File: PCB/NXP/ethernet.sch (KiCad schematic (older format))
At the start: 40 parts, among them P1 HR911105A, U1 LAN8720A-CP, U2 SI502

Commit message: #45 added PoE connector (P1) and expansion (P3).
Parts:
- removed P1: HR911105A, symbol CONN_14
- added P1: SI-52003-F, ~, symbol CONN_17
- added P3: PoE, ~, symbol CONN_7
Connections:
- net labels added: +24V, +5V
- wire segments 114 -> 131
- no-connect marks 2 -> 3
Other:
- note added: "Se agregan entradas de +5V y +24V para alimentar la CIAA\na través de PoE. Es necesario diseñar una expansión tal que, \nademás de la fuente de tensión, disponga de diodos de \nprotección para no dañarla si se alimenta la CIAA en forma \ntradicional. Se sugiere usar diodos PMEG3020EH como en la \nfuente de alimentación. A su vez es necesario que cada entrada\nPoE tenga un puente rectificador de o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"
- note added: "TD+\nCT\nTD-\nRD+\nRD-\nNC\nNC\nVC+\nVC-\nVC+\nVC-\nLED1_A\nLED1_K\nLED2_A\nLED2_K\nSHIELD\nSHIELD"
- note removed: "Verificar disponibilidad del conector Ethernet.\nAlternativa: Pulse J0011D01BNL."
- moved on the sheet: R17, R18
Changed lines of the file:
@@
 Sheet 3 12
 Title "CIAA Ethernet"
-Date "18 aug 2014"
+Date "19 aug 2014"
 Rev "1.0"
 Comp ""
@@
 $EndComp
 $Comp
-L CONN_14 P1
-U 1 1 529F7478
-P 10000 3950
-F 0 "P1" V 9970 3950 60  0000 C CNN
-F 1 "HR911105A" V 10080 3950 60  0000 C CNN
-F 2 "" H 10000 3950 60  0000 C CNN
-F 3 "" H 10000 3950 60  0000 C CNN
-	1    10000 3950
-	1    0    0    -1
-$EndComp
-$Comp
 L R R3
 U 1 1 529F75AC
@@
 	7100 3900 7550 3900
 Wire Wire Line
-	7550 3900 7550 3400
-Wire Wire Line
-	7550 3400 9650 3400
+	7550 3900 7550 3500
+Wire Wire Line
+	7550 3500 9650 3500
 Wire Wire Line
 	7100 4000 7650 4000
 Wire Wire Line
-	7650 3500 7650 4300
-Wire Wire Line
-	7650 3500 9650 3500
-Wire Wire Line
 	7100 4100 7750 4100
 Wire Wire Line
-	7750 4100 7750 3800
-Wire Wire Line
-	7750 3800 9650 3800
-Wire Wire Line
-	9550 3700 9650 3700
-Wire Wire Line
-	9550 2600 9550 3700
-Wire Wire Line
-	9550 3600 9650 3600
+	7750 4100 7750 3700
+Wire Wire Line
+	7750 3700 9650 3700
 Wire Wire Line
 	7450 1600 7450 2600
 Wire Wire Line
-	7450 2600 9550 2600
-Connection ~ 9550 3600
+	7450 2600 9450 2600
 Connection ~ 6150 1600
 Wire Wire Line
@@
 Connection ~ 8100 2600
 Wire Wire Line
-	8100 3150 8100 3400
-Connection ~ 8100 3400
+	8100 3150 8100 3500
+Connection ~ 8100 3500
 Wire Wire Line
 	8350 2700 8350 2600
@@
 Connection ~ 8700 2600
 Wire Wire Line
-	8700 3150 8700 3500
-Connection ~ 8700 3500
-Wire Wire Line
-	8900 3150 8900 3800
-Connection ~ 8900 3800
+	8900 3150 8900 3700
+Connection ~ 8900 3700
 Wire Wire Line
 	9150 3150 9150 3100
@@
 	7400 4300 7400 3900
 Connection ~ 7400 3900
-Connection ~ 7650 4000
-Wire Wire Line
-	7900 4300 7900 3800
-Connection ~ 7900 3800
-NoConn ~ 9650 3900
-Wire Wire Line
-	9450 4000 9650 4000
-Wire Wire Line
-	9450 4600 9650 4600
-Connection ~ 9450 4600
-Wire Wire Line
-	9650 4500 9450 4500
-Connection ~ 9450 4500
+Wire Wire Line
+	7900 4300 7900 3700
+Connection ~ 7900 3700
+NoConn ~ 9650 3800
 $Comp
 L GND #PWR078
 U 1 1 529F7D8C
-P 9450 4750
-F 0 "#PWR078" H 9450 4750 30  0001 C CNN
-F 1 "GND" H 9450 4680 30  0001 C CNN
-F 2 "" H 9450 4750 60  0000 C CNN
-F 3 "" H 9450 4750 60  0000 C CNN
-	1    9450 4750
-	1    0    0    -1
-$EndComp
-Wire Wire Line
-	9450 4000 9450 4750
-Wire Wire Line
-	9650 4400 8850 4400
-Wire Wire Line
-	9650 4100 8850 4100
-Text Label 8700 4300 0    60   ~ 0
+P 9350 5000
+F 0 "#PWR078" H 9350 5000 30  0001 C CNN
+F 1 "GND" H 9350 4930 30  0001 C CNN
+F 2 "" H 9350 5000 60  0000 C CNN
+F 3 "" H 9350 5000 60  0000 C CNN
+	1    9350 5000
+	1    0    0    -1
+$EndComp
+Wire Wire Line
+	9650 4400 8950 4400
+Text Label 8950 4700 0    60   ~ 0
 LED_100M
-Text Label 8850 4100 0    60   ~ 0
+Text Label 8950 4400 0    60   ~ 0
 LED_LINK
 $Comp
 L R R17
 U 1 1 529F7EB8
-P 8500 4550
-F 0 "R17" V 8580 4550 40  0000 C CNN
-F 1 "270" V 8507 4551 40  0000 C CNN
-F 2 "~" V 8430 4550 30  0000 C CNN
-F 3 "~" H 8500 4550 30  0000 C CNN
-	1    8500 4550
+P 8650 4850
+F 0 "R17" V 8730 4850 40  0000 C CNN
+F 1 "270" V 8657 4851 40  0000 C CNN
+F 2 "~" V 8580 4850 30  0000 C CNN
+F 3 "~" H 8650 4850 30  0000 C CNN
+	1    8650 4850
 	-1   0    0    1
 $EndComp
@@
 L R R18
 U 1 1 529F7EC7
-P 8850 4650
-F 0 "R18" V 8930 4650 40  0000 C CNN
-F 1 "270" V 8857 4651 40  0000 C CNN
-F 2 "~" V 8780 4650 30  0000 C CNN
-F 3 "~" H 8850 4650 30  0000 C CNN
-	1    8850 4650
-	-1   0    0    1
-$EndComp
-Wire Wire Line
-	9650 4200 8500 4200
-Wire Wire Line
-	8500 4200 8500 4300
-Wire Wire Line
-	8700 4300 9650 4300
-Wire Wire Line
-	8500 4800 8500 4850
+P 8800 4850
+F 0 "R18" V 8880 4850 40  0000 C CNN
+F 1 "270" V 8807 4851 40  0000 C CNN
+F 2 "~" V 8730 4850 30  0000 C CNN
+F 3 "~" H 8800 4850 30  0000 C CNN
+	1    8800 4850
+	1    0    0    -1
+$EndComp
+Wire Wire Line
+	9650 4500 8650 4500
+Wire Wire Line
+	8650 4500 8650 4600
+Wire Wire Line
+	8950 4700 9650 4700
+Wire Wire Line
+	8650 5100 8650 5150
 $Comp
 L GND #PWR079
 U 1 1 529F808F
-P 8500 4850
-F 0 "#PWR079" H 8500 4850 30  0001 C CNN
-F 1 "GND" H 8500 4780 30  0001 C CNN
-F 2 "" H 8500 4850 60  0000 C CNN
-F 3 "" H 8500 4850 60  0000 C CNN
-	1    8500 4850
+P 8650 5150
+F 0 "#PWR079" H 8650 5150 30  0001 C CNN
+F 1 "GND" H 8650 5080 30  0001 C CNN
+F 2 "" H 8650 5150 60  0000 C CNN
+F 3 "" H 8650 5150 60  0000 C CNN
+	1    8650 5150
 	1    0    0    -1
 $EndComp
@@
 L +3.3V #PWR089
 U 1 1 52C68806
-P 9050 4900
-F 0 "#PWR089" H 9050 4860 30  0001 C CNN
-F 1 "+3.3V" H 9050 5010 30  0000 C CNN
-F 2 "" H 9050 4900 60  0000 C CNN
-F 3 "" H 9050 4900 60  0000 C CNN
-	1    9050 4900
-	1    0    0    -1
-$EndComp
-Wire Wire Line
-	8850 4900 9050 4900
+P 8900 5150
+F 0 "#PWR089" H 8900 5110 30  0001 C CNN
+F 1 "+3.3V" H 8900 5260 30  0000 C CNN
+F 2 "" H 8900 5150 60  0000 C CNN
+F 3 "" H 8900 5150 60  0000 C CNN
+	1    8900 5150
+	1    0    0    -1
+$EndComp
 $Comp
 L CP1 C5
@@
 	1    0    0    -1
 $EndComp
-Text Notes 8850 5100 0    60   ~ 12
-Verificar disponibilidad del conector Ethernet.\nAlternativa: Pulse J0011D01BNL.
+Wire Wire Line
+	9650 3400 9450 3400
+Wire Wire Line
+	9450 3400 9450 2600
+Wire Wire Line
+	7650 3600 9650 3600
+Wire Wire Line
+	7650 3600 7650 4300
+Wire Wire Line
+	8700 3150 8700 3600
+Connection ~ 8700 3600
+Connection ~ 7650 4000
+NoConn ~ 9650 3900
+$Comp
+L CONN_17 P1
+U 1 1 53F384B4
+P 10000 4100
+F 0 "P1" V 9960 4100 60  0000 C CNN
+F 1 "SI-52003-F" V 10080 4100 60  0000 C CNN
+F 2 "~" H 10000 4100 60  0000 C CNN
+F 3 "~" H 10000 4100 60  0000 C CNN
+	1    10000 4100
+	1    0    0    -1
+$EndComp
+Wire Wire Line
+	9650 4300 9600 4300
+Wire Wire Line
+	9600 4300 9600 5150
+Wire Wire Line
+	9600 5150 9650 5150
+Wire Wire Line
+	9650 5250 9550 5250
+Wire Wire Line
+	9550 5250 9550 4200
+Wire Wire Line
+	9550 4200 9650 4200
+Wire Wire Line
+	9650 4100 9500 4100
+Wire Wire Line
+	9500 4100 9500 5350
+Wire Wire Line
+	9500 5350 9650 5350
+Wire Wire Line
+	9650 5450 9450 5450
+Wire Wire Line
+	9450 5450 9450 4000
+Wire Wire Line
+	9450 4000 9650 4000
+Wire Wire Line
+	9350 4800 9350 5000
+Wire Wire Line
+	9350 4900 9650 4900
+Wire Wire Line
+	9650 4800 9350 4800
+Connection ~ 9350 4900
+Wire Wire Line
+	8800 5150 8900 5150
+Wire Wire Line
+	8800 5150 8800 5100
+Wire Wire Line
+	9650 4600 8800 4600
+Text Notes 10150 3350 0    71   ~ 0
+TD+\nCT\nTD-\nRD+\nRD-\nNC\nNC\nVC+\nVC-\nVC+\nVC-\nLED1_A\nLED1_K\nLED2_A\nLED2_K\nSHIELD\nSHIELD
+$Comp
+L +5V #PWR090
+U 1 1 53F3EF9C
+P 9350 5450
+F 0 "#PWR090" H 9350 5540 20  0001 C CNN
+F 1 "+5V" H 9350 5540 30  0000 C CNN
+F 2 "" H 9350 5450 60  0000 C CNN
+F 3 "" H 9350 5450 60  0000 C CNN
+	1    9350 5450
+	1    0    0    -1
+$EndComp
+Wire Wire Line
+	9350 5450 9350 5550
+Wire Wire Line
+	9350 5550 9650 5550
+$Comp
+L +24V #PWR091
+U 1 1 53F3F79C
+P 9200 5450
+F 0 "#PWR091" H 9200 5400 20  0001 C CNN
+F 1 "+24V" H 9200 5550 30  0000 C CNN
+F 2 "" H 9200 5450 60  0000 C CNN
+F 3 "" H 9200 5450 60  0000 C CNN
+	1    9200 5450
+	1    0    0    -1
+$EndComp
+Wire Wire Line
+	9200 5450 9200 5650
+Wire Wire Line
+	9200 5650 9650 5650
+Text Notes 8100 6100 0    60   ~ 0
+Se agregan entradas de +5V y +24V para alimentar la CIAA\na través de PoE. Es necesario diseñar una expansión tal que, \nademás de la fuente de tensión, disponga de diodos de \nprotección para no dañarla si se alimenta la CIAA en forma \ntradicional. Se sugiere usar diodos PMEG3020EH como en la \nfuente de alimentación. A su vez es necesario que cada entrada\nPoE tenga un puente rectificador de onda completa ya que la \nnorma no determina polaridad. Ver por ejemplo el módulo PoE\nAG9605-2BR.
+$Comp
+L CONN_7 P3
+U 1 1 53F3CD51
+P 10000 5450
+F 0 "P3" V 9970 5450 60  0000 C CNN
+F 1 "PoE" V 10070 5450 60  0000 C CNN
+F 2 "~" H 10000 5450 60  0000 C CNN
+F 3 "~" H 10000 5450 60  0000 C CNN
+	1    10000 5450
+	1    0    0    -1
+$EndComp
+$Comp
+L GND #PWR092
+U 1 1 53F3CD68
+P 9450 5800
+F 0 "#PWR092" H 9450 5800 30  0001 C CNN
+F 1 "GND" H 9450 5730 30  0001 C CNN
+F 2 "" H 9450 5800 60  0000 C CNN
+F 3 "" H 9450 5800 60  0000 C CNN
+	1    9450 5800
+	1    0    0    -1
+$EndComp
+Wire Wire Line
+	9650 5750 9450 5750
+Wire Wire Line
+	9450 5750 9450 5800
 $EndSCHEMATC

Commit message: #45 P3 enhanced.
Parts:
- removed P3: PoE, ~, symbol CONN_7
- added P3: PoE, ~, symbol CONN_4X2
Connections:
- wire segments 131 -> 135
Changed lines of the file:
@@
 	9650 4300 9600 4300
 Wire Wire Line
-	9600 4300 9600 5150
-Wire Wire Line
-	9600 5150 9650 5150
-Wire Wire Line
-	9650 5250 9550 5250
-Wire Wire Line
-	9550 5250 9550 4200
+	9600 4300 9600 5100
 Wire Wire Line
 	9550 4200 9650 4200
 Wire Wire Line
 	9650 4100 9500 4100
-Wire Wire Line
-	9500 4100 9500 5350
-Wire Wire Line
-	9500 5350 9650 5350
-Wire Wire Line
-	9650 5450 9450 5450
-Wire Wire Line
-	9450 5450 9450 4000
 Wire Wire Line
 	9450 4000 9650 4000
@@
 L +5V #PWR090
 U 1 1 53F3EF9C
-P 9350 5450
-F 0 "#PWR090" H 9350 5540 20  0001 C CNN
-F 1 "+5V" H 9350 5540 30  0000 C CNN
-F 2 "" H 9350 5450 60  0000 C CNN
-F 3 "" H 9350 5450 60  0000 C CNN
-	1    9350 5450
+P 10750 5450
+F 0 "#PWR090" H 10750 5540 20  0001 C CNN
+F 1 "+5V" H 10750 5540 30  0000 C CNN
+F 2 "" H 10750 5450 60  0000 C CNN
+F 3 "" H 10750 5450 60  0000 C CNN
+	1    10750 5450
+	1    0    0    -1
+$EndComp
+$Comp
+L +24V #PWR091
+U 1 1 53F3F79C
+P 10600 5450
+F 0 "#PWR091" H 10600 5400 20  0001 C CNN
+F 1 "+24V" H 10600 5550 30  0000 C CNN
+F 2 "" H 10600 5450 60  0000 C CNN
+F 3 "" H 10600 5450 60  0000 C CNN
+	1    10600 5450
+	1    0    0    -1
+$EndComp
+Text Notes 8100 6100 0    60   ~ 0
+Se agregan entradas de +5V y +24V para alimentar la CIAA\na través de PoE. Es necesario diseñar una expansión tal que, \nademás de la fuente de tensión, disponga de diodos de \nprotección para no dañarla si se alimenta la CIAA en forma \ntradicional. Se sugiere usar diodos PMEG3020EH como en la \nfuente de alimentación. A su vez es necesario que cada entrada\nPoE tenga un puente rectificador de onda completa ya que la \nnorma no determina polaridad. Ver por ejemplo el módulo PoE\nAG9605-2BR.
+$Comp
+L GND #PWR092
+U 1 1 53F3CD68
+P 9600 5700
+F 0 "#PWR092" H 9600 5700 30  0001 C CNN
+F 1 "GND" H 9600 5630 30  0001 C CNN
+F 2 "" H 9600 5700 60  0000 C CNN
+F 3 "" H 9600 5700 60  0000 C CNN
+	1    9600 5700
 	1    0    0    -1
 $EndComp
 Wire Wire Line
-	9350 5450 9350 5550
-Wire Wire Line
-	9350 5550 9650 5550
+	9600 5550 9600 5700
 $Comp
-L +24V #PWR091
-U 1 1 53F3F79C
-P 9200 5450
-F 0 "#PWR091" H 9200 5400 20  0001 C CNN
-F 1 "+24V" H 9200 5550 30  0000 C CNN
-F 2 "" H 9200 5450 60  0000 C CNN
-F 3 "" H 9200 5450 60  0000 C CNN
-	1    9200 5450
+L CONN_4X2 P3
+U 1 1 53F39CAF
+P 10050 5500
+F 0 "P3" H 10050 5750 50  0000 C CNN
+F 1 "PoE" V 10050 5500 40  0000 C CNN
+F 2 "~" H 10050 5500 60  0000 C CNN
+F 3 "~" H 10050 5500 60  0000 C CNN
+	1    10050 5500
 	1    0    0    -1
 $EndComp
 Wire Wire Line
-	9200 5450 9200 5650
+	9450 4000 9450 5350
 Wire Wire Line
-	9200 5650 9650 5650
-Text Notes 8100 6100 0    60   ~ 0
-Se agregan entradas de +5V y +24V para alimentar la CIAA\na través de PoE. Es necesario diseñar una expansión tal que, \nademás de la fuente de tensión, disponga de diodos de \nprotección para no dañarla si se alimenta la CIAA en forma \ntradicional. Se sugiere usar diodos PMEG3020EH como en la \nfuente de alimentación. A su vez es necesario que cada entrada\nPoE tenga un puente rectificador de onda completa ya que la \nnorma no determina polaridad. Ver por ejemplo el módulo PoE\nAG9605-2BR.
-$Comp
-L CONN_7 P3
-U 1 1 53F3CD51
-P 10000 5450
-F 0 "P3" V 9970 5450 60  0000 C CNN
-F 1 "PoE" V 10070 5450 60  0000 C CNN
-F 2 "~" H 10000 5450 60  0000 C CNN
-F 3 "~" H 10000 5450 60  0000 C CNN
-	1    10000 5450
-	1    0    0    -1
-$EndComp
-$Comp
-L GND #PWR092
-U 1 1 53F3CD68
-P 9450 5800
-F 0 "#PWR092" H 9450 5800 30  0001 C CNN
-F 1 "GND" H 9450 5730 30  0001 C CNN
-F 2 "" H 9450 5800 60  0000 C CNN
-F 3 "" H 9450 5800 60  0000 C CNN
-	1    9450 5800
-	1    0    0    -1
-$EndComp
+	9450 5350 9650 5350
 Wire Wire Line
-	9650 5750 9450 5750
+	10450 5150 10450 5350
 Wire Wire Line
-	9450 5750 9450 5800
+	10500 5100 10500 5450
+Wire Wire Line
+	10500 5450 10450 5450
+Wire Wire Line
+	9500 4100 9500 5150
+Wire Wire Line
+	9500 5150 10450 5150
+Wire Wire Line
+	9550 5450 9650 5450
+Wire Wire Line
+	9600 5100 10500 5100
+Wire Wire Line
+	9550 4200 9550 5450
+Wire Wire Line
+	9600 5550 9650 5550
+Wire Wire Line
+	10600 5450 10600 5550
+Wire Wire Line
+	10600 5550 10450 5550
+Wire Wire Line
+	10450 5650 10750 5650
+Wire Wire Line
+	10750 5650 10750 5450
+Connection ~ 9600 5650
+Wire Wire Line
+	9600 5650 9650 5650
 $EndSCHEMATC

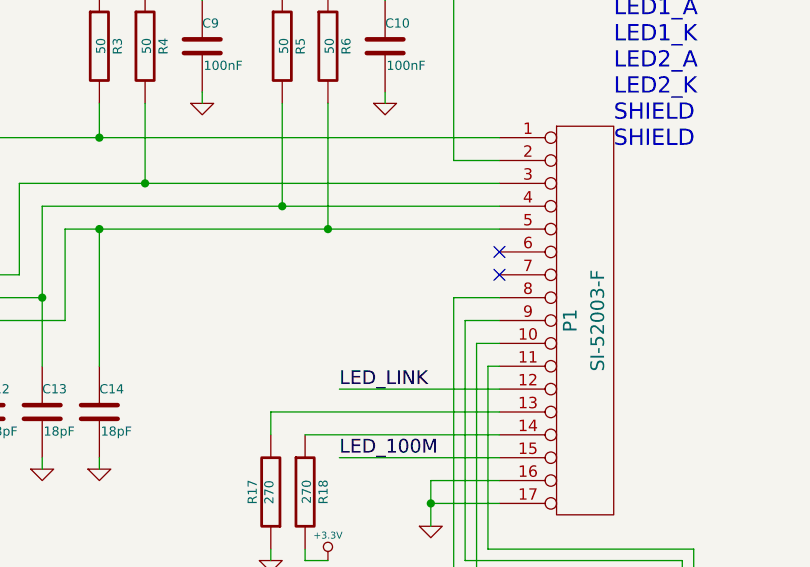
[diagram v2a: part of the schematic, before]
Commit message: gerbers generados y actualizada la descripción del PCB
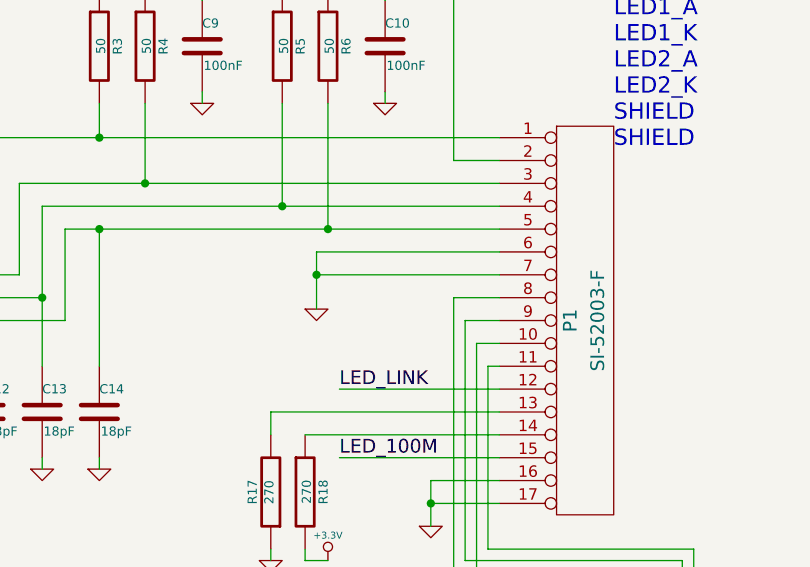
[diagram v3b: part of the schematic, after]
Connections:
- wire segments 135 -> 138
- no-connect marks 3 -> 1
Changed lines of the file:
@@
 Sheet 3 12
 Title "CIAA Ethernet"
-Date "19 aug 2014"
+Date "29 sep 2014"
 Rev "1.0"
 Comp ""
@@
 	7900 4300 7900 3700
 Connection ~ 7900 3700
-NoConn ~ 9650 3800
 $Comp
 L GND #PWR078
@@
 Connection ~ 8700 3600
 Connection ~ 7650 4000
-NoConn ~ 9650 3900
 $Comp
 L CONN_17 P1
@@
 Wire Wire Line
 	9600 5650 9650 5650
+$Comp
+L GND #PWR?
+U 1 1 5429B31A
+P 8850 4050
+F 0 "#PWR?" H 8850 4050 30  0001 C CNN
+F 1 "GND" H 8850 3980 30  0001 C CNN
+F 2 "" H 8850 4050 60  0000 C CNN
+F 3 "" H 8850 4050 60  0000 C CNN
+	1    8850 4050
+	1    0    0    -1
+$EndComp
+Wire Wire Line
+	8850 3800 8850 4050
+Wire Wire Line
+	9650 3800 8850 3800
+Wire Wire Line
+	9650 3900 8850 3900
+Connection ~ 8850 3900
 $EndSCHEMATC

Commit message: [ciaa-nxp] schematic layout fixed for newer versions of kicad
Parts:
- C1, C5: symbol CP1 -> CP1-RESCUE-ciaa-nxp
- C10, C11, C12, C13, C14, C15, C2, C3, C4, C6, C7, C8, C9: symbol C -> C-RESCUE-ciaa-nxp
- R1, R10, R11, R12, R13, R14, R15, R16, R17, R18, R19, R2, R20, R21, R3, R4, R5, R6, R7, R8, R9: symbol R -> R-RESCUE-ciaa-nxp
- U2: symbol SI50X -> Si50X
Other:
- moved on the sheet: C1, C10, C11, C12, C13, C14, C15, C2, C3, C4, C5, C6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
